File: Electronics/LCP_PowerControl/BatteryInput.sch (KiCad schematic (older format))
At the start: 0 parts

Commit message: Adding libraries and recent changes
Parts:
- added D?: D, symbol Device:D
- added J? (x5): Conn_01x02, Connector_PinSocket_2.54mm:PinSocket_1x02_P2.54mm_Vertical, symbol Connector_Generic:Conn_01x02
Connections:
- net BATT_V+: now also D?.1 (K), J?.2 (Pin_2), J?.2 (Pin_2), J?.2 (Pin_2), J?.2 (Pin_2)
- new net: D?.2 (A), J?.2 (Pin_2)
- new net GND: J?.1 (Pin_1), J?.1 (Pin_1), J?.1 (Pin_1), J?.1 (Pin_1), J?.1 (Pin_1)
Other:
- note added: "Battery #1 Connector"
- note added: "Battery #2 Connector"
- note added: "Battery #3 Connector"
- note added: "Battery #4 Connector"
- note added: "Battery Connections:\nExpected Battery Pack\n18SP1 Stacks, Alkaline, Diode Protected"
- note added: "External Power Connector\n(DC Supply)"
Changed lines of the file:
@@
 $Descr A4 11693 8268
 encoding utf-8
-Sheet 2 8
+Sheet 2 11
 Title ""
 Date ""
@@
 Comment4 ""
 $EndDescr
-Text HLabel 9500 2400 2    50   Output ~ 0
+Text HLabel 9600 1850 2    50   Output ~ 0
 BATT_V+
-Text HLabel 9500 2750 2    50   Input ~ 0
+Text HLabel 9600 1950 2    50   Input ~ 0
 BATT_V-
+$Comp
+L Connector_Generic:Conn_01x02 J?
+U 1 1 5EF29935
+P 3900 1950
+F 0 "J?" H 3818 1625 50  0000 C CNN
+F 1 "Conn_01x02" H 3818 1716 50  0000 C CNN
+F 2 "Connector_PinSocket_2.54mm:PinSocket_1x02_P2.54mm_Vertical" H 3900 1950 50  0001 C CNN
+F 3 "~" H 3900 1950 50  0001 C CNN
+	1    3900 1950
+	-1   0    0    1
+$EndComp
+$Comp
+L Connector_Generic:Conn_01x02 J?
+U 1 1 5EF2A22F
+P 3900 2850
+F 0 "J?" H 3818 2525 50  0000 C CNN
+F 1 "Conn_01x02" H 3818 2616 50  0000 C CNN
+F 2 "Connector_PinSocket_2.54mm:PinSocket_1x02_P2.54mm_Vertical" H 3900 2850 50  0001 C CNN
+F 3 "~" H 3900 2850 50  0001 C CNN
+	1    3900 2850
+	-1   0    0    1
+$EndComp
+$Comp
+L Connector_Generic:Conn_01x02 J?
+U 1 1 5EF2A6FE
+P 3900 3850
+F 0 "J?" H 3818 3525 50  0000 C CNN
+F 1 "Conn_01x02" H 3818 3616 50  0000 C CNN
+F 2 "Connector_PinSocket_2.54mm:PinSocket_1x02_P2.54mm_Vertical" H 3900 3850 50  0001 C CNN
+F 3 "~" H 3900 3850 50  0001 C CNN
+	1    3900 3850
+	-1   0    0    1
+$EndComp
+$Comp
+L Connector_Generic:Conn_01x02 J?
+U 1 1 5EF2AC09
+P 3900 4850
+F 0 "J?" H 3818 4525 50  0000 C CNN
+F 1 "Conn_01x02" H 3818 4616 50  0000 C CNN
+F 2 "Connector_PinSocket_2.54mm:PinSocket_1x02_P2.54mm_Vertical" H 3900 4850 50  0001 C CNN
+F 3 "~" H 3900 4850 50  0001 C CNN
+	1    3900 4850
+	-1   0    0    1
+$EndComp
+$Comp
+L Connector_Generic:Conn_01x02 J?
+U 1 1 5EF2B236
+P 3900 5950
+F 0 "J?" H 3818 5625 50  0000 C CNN
+F 1 "Conn_01x02" H 3818 5716 50  0000 C CNN
+F 2 "Connector_PinSocket_2.54mm:PinSocket_1x02_P2.54mm_Vertical" H 3900 5950 50  0001 C CNN
+F 3 "~" H 3900 5950 50  0001 C CNN
+	1    3900 5950
+	-1   0    0    1
+$EndComp
+$Comp
+L Device:D D?
+U 1 1 5EF2F687
+P 5150 5850
+F 0 "D?" H 5150 6066 50  0000 C CNN
+F 1 "D" H 5150 5975 50  0000 C CNN
+F 2 "" H 5150 5850 50  0001 C CNN
+F 3 "~" H 5150 5850 50  0001 C CNN
+	1    5150 5850
+	-1   0    0    -1
+$EndComp
+Wire Wire Line
+	4100 5950 4450 5950
+Wire Wire Line
+	4450 5950 4450 4850
+Wire Wire Line
+	4450 1950 4100 1950
+Wire Wire Line
+	4100 2850 4450 2850
+Connection ~ 4450 2850
+Wire Wire Line
+	4450 2850 4450 1950
+Wire Wire Line
+	4100 3850 4450 3850
+Connection ~ 4450 3850
+Wire Wire Line
+	4450 3850 4450 2850
+Wire Wire Line
+	4100 4850 4450 4850
+Connection ~ 4450 4850
+Wire Wire Line
+	4450 4850 4450 3850
+$Comp
+L power:GND #PWR?
+U 1 1 5EF31DCF
+P 4450 6300
+F 0 "#PWR?" H 4450 6050 50  0001 C CNN
+F 1 "GND" H 4455 6127 50  0000 C CNN
+F 2 "" H 4450 6300 50  0001 C CNN
+F 3 "" H 4450 6300 50  0001 C CNN
+	1    4450 6300
+	1    0    0    -1
+$EndComp
+Wire Wire Line
+	4450 6300 4450 5950
+Connection ~ 4450 5950
+Wire Wire Line
+	4100 5850 5000 5850
+Wire Wire Line
+	4100 4750 5650 4750
+Wire Wire Line
+	5650 4750 5650 5850
+Wire Wire Line
+	5650 5850 5300 5850
+Wire Wire Line
+	4100 3750 5650 3750
+Wire Wire Line
+	5650 3750 5650 4750
+Connection ~ 5650 4750
+Wire Wire Line
+	5650 2750 5650 3750
+Connection ~ 5650 3750
+Wire Wire Line
+	4100 2750 5650 2750
+Wire Wire Line
+	4100 1850 5650 1850
+Connection ~ 5650 2750
+Wire Wire Line
+	9600 1850 5650 1850
+Connection ~ 5650 1850
+Wire Wire Line
+	5650 1850 5650 2750
+Wire Wire Line
+	9600 1950 4450 1950
+Connection ~ 4450 1950
+Text Notes 2650 5950 0    50   ~ 0
+External Power Connector\n(DC Supply)
+Text Notes 2850 1950 0    50   ~ 0
+Battery #1 Connector
+Text Notes 2850 2850 0    50   ~ 0
+Battery #2 Connector
+Text Notes 2850 3800 0    50   ~ 0
+Battery #3 Connector
+Text Notes 2850 4800 0    50   ~ 0
+Battery #4 Connector
+Text Notes 1050 1300 0    50   ~ 0
+Battery Connections:\nExpected Battery Pack\n18SP1 Stacks, Alkaline, Diode Protected
 $EndSCHEMATC

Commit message: Aiming for rev 0.1 complete
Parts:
- added TP22, TP23: TestPoint, TestPoint:TestPoint_Keystone_5000-5004_Miniature, symbol Connector:TestPoint
- D5: renamed from D?; footprint (none) -> Diode_SMD:D_SMA; MPN (none) -> SK53A-LTP
- J10, J11, J12, J3, J9: renamed from J?; footprint Connector_PinSocket_2.54mm:PinSocket_1x02_P2.54mm_Vertical -> Connector_Molex:Molex_Micro-Fit_3.0_43045-0200_2x01_P3.00mm_Horizontal
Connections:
- net BATT_V+: now also TP22.1
- net GND: now also TP23.1
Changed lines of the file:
@@
 Sheet 2 11
 Title ""
-Date ""
-Rev ""
+Date "2020-06-17"
+Rev "R0.1"
 Comp ""
-Comment1 ""
+Comment1 "Design by: Matt Casari"
 Comment2 ""
 Comment3 ""
@@
 BATT_V-
 $Comp
-L Connector_Generic:Conn_01x02 J?
+L Connector_Generic:Conn_01x02 J3
 U 1 1 5EF29935
 P 3900 1950
-F 0 "J?" H 3818 1625 50  0000 C CNN
+F 0 "J3" H 3818 1625 50  0000 C CNN
 F 1 "Conn_01x02" H 3818 1716 50  0000 C CNN
-F 2 "Connector_PinSocket_2.54mm:PinSocket_1x02_P2.54mm_Vertical" H 3900 1950 50  0001 C CNN
+F 2 "Connector_Molex:Molex_Micro-Fit_3.0_43045-0200_2x01_P3.00mm_Horizontal" H 3900 1950 50  0001 C CNN
 F 3 "~" H 3900 1950 50  0001 C CNN
 	1    3900 1950
@@
 $EndComp
 $Comp
-L Connector_Generic:Conn_01x02 J?
+L Connector_Generic:Conn_01x02 J9
 U 1 1 5EF2A22F
 P 3900 2850
-F 0 "J?" H 3818 2525 50  0000 C CNN
+F 0 "J9" H 3818 2525 50  0000 C CNN
 F 1 "Conn_01x02" H 3818 2616 50  0000 C CNN
-F 2 "Connector_PinSocket_2.54mm:PinSocket_1x02_P2.54mm_Vertical" H 3900 2850 50  0001 C CNN
+F 2 "Connector_Molex:Molex_Micro-Fit_3.0_43045-0200_2x01_P3.00mm_Horizontal" H 3900 2850 50  0001 C CNN
 F 3 "~" H 3900 2850 50  0001 C CNN
 	1    3900 2850
@@
 $EndComp
 $Comp
-L Connector_Generic:Conn_01x02 J?
+L Connector_Generic:Conn_01x02 J10
 U 1 1 5EF2A6FE
 P 3900 3850
-F 0 "J?" H 3818 3525 50  0000 C CNN
+F 0 "J10" H 3818 3525 50  0000 C CNN
 F 1 "Conn_01x02" H 3818 3616 50  0000 C CNN
-F 2 "Connector_PinSocket_2.54mm:PinSocket_1x02_P2.54mm_Vertical" H 3900 3850 50  0001 C CNN
+F 2 "Connector_Molex:Molex_Micro-Fit_3.0_43045-0200_2x01_P3.00mm_Horizontal" H 3900 3850 50  0001 C CNN
 F 3 "~" H 3900 3850 50  0001 C CNN
 	1    3900 3850
@@
 $EndComp
 $Comp
-L Connector_Generic:Conn_01x02 J?
+L Connector_Generic:Conn_01x02 J11
 U 1 1 5EF2AC09
 P 3900 4850
-F 0 "J?" H 3818 4525 50  0000 C CNN
+F 0 "J11" H 3818 4525 50  0000 C CNN
 F 1 "Conn_01x02" H 3818 4616 50  0000 C CNN
-F 2 "Connector_PinSocket_2.54mm:PinSocket_1x02_P2.54mm_Vertical" H 3900 4850 50  0001 C CNN
+F 2 "Connector_Molex:Molex_Micro-Fit_3.0_43045-0200_2x01_P3.00mm_Horizontal" H 3900 4850 50  0001 C CNN
 F 3 "~" H 3900 4850 50  0001 C CNN
 	1    3900 4850
@@
 $EndComp
 $Comp
-L Connector_Generic:Conn_01x02 J?
+L Connector_Generic:Conn_01x02 J12
 U 1 1 5EF2B236
 P 3900 5950
-F 0 "J?" H 3818 5625 50  0000 C CNN
+F 0 "J12" H 3818 5625 50  0000 C CNN
 F 1 "Conn_01x02" H 3818 5716 50  0000 C CNN
-F 2 "Connector_PinSocket_2.54mm:PinSocket_1x02_P2.54mm_Vertical" H 3900 5950 50  0001 C CNN
+F 2 "Connector_Molex:Molex_Micro-Fit_3.0_43045-0200_2x01_P3.00mm_Horizontal" H 3900 5950 50  0001 C CNN
 F 3 "~" H 3900 5950 50  0001 C CNN
 	1    3900 5950
@@
 $EndComp
 $Comp
-L Device:D D?
+L Device:D D5
 U 1 1 5EF2F687
 P 5150 5850
-F 0 "D?" H 5150 6066 50  0000 C CNN
+F 0 "D5" H 5150 6066 50  0000 C CNN
 F 1 "D" H 5150 5975 50  0000 C CNN
-F 2 "" H 5150 5850 50  0001 C CNN
+F 2 "Diode_SMD:D_SMA" H 5150 5850 50  0001 C CNN
 F 3 "~" H 5150 5850 50  0001 C CNN
+F 4 "SK53A-LTP" H 5150 5850 50  0001 C CNN "MPN"
 	1    5150 5850
 	-1   0    0    -1
@@
 	4450 4850 4450 3850
 $Comp
-L power:GND #PWR?
+L power:GND #PWR015
 U 1 1 5EF31DCF
 P 4450 6300
-F 0 "#PWR?" H 4450 6050 50  0001 C CNN
+F 0 "#PWR015" H 4450 6050 50  0001 C CNN
 F 1 "GND" H 4455 6127 50  0000 C CNN
 F 2 "" H 4450 6300 50  0001 C CNN
@@
 	4100 1850 5650 1850
 Connection ~ 5650 2750
-Wire Wire Line
-	9600 1850 5650 1850
 Connection ~ 5650 1850
 Wire Wire Line
 	5650 1850 5650 2750
-Wire Wire Line
-	9600 1950 4450 1950
 Connection ~ 4450 1950
 Text Notes 2650 5950 0    50   ~ 0
@@
 Text Notes 1050 1300 0    50   ~ 0
 Battery Connections:\nExpected Battery Pack\n18SP1 Stacks, Alkaline, Diode Protected
+$Comp
+L Connector:TestPoint TP?
+U 1 1 5F052069
+P 6600 1600
+AR Path="/5EE2A7AF/5F052069" Ref="TP?"  Part="1"
+AR Path="/5EE4388C/5F052069" Ref="TP?"  Part="1"
+AR Path="/5EE2A57D/5F052069" Ref="TP22"  Part="1"
+F 0 "TP22" H 6658 1718 50  0000 L CNN
+F 1 "TestPoint" H 6658 1627 50  0000 L CNN
+F 2 "TestPoint:TestPoint_Keystone_5000-5004_Miniature" H 6800 1600 50  0001 C CNN
+F 3 "~" H 6800 1600 50  0001 C CNN
+F 4 "5000" H 6600 1600 50  0001 C CNN "MPN"
+	1    6600 1600
+	1    0    0    -1
+$EndComp
+$Comp
+L Connector:TestPoint TP?
+U 1 1 5F052070
+P 7050 1600
+AR Path="/5EE2A7AF/5F052070" Ref="TP?"  Part="1"
+AR Path="/5EE4388C/5F052070" Ref="TP?"  Part="1"
+AR Path="/5EE2A57D/5F052070" Ref="TP23"  Part="1"
+F 0 "TP23" H 7108 1718 50  0000 L CNN
+F 1 "TestPoint" H 7108 1627 50  0000 L CNN
+F 2 "TestPoint:TestPoint_Keystone_5000-5004_Miniature" H 7250 1600 50  0001 C CNN
+F 3 "~" H 7250 1600 50  0001 C CNN
+F 4 "5001" H 7050 1600 50  0001 C CNN "MPN"
+	1    7050 1600
+	1    0    0    -1
+$EndComp
+Wire Wire Line
+	6600 1600 6600 1850
+Wire Wire Line
+	5650 1850 6600 1850
+Connection ~ 6600 1850
+Wire Wire Line
+	6600 1850 9600 1850
+Wire Wire Line
+	7050 1600 7050 1950
+Wire Wire Line
+	4450 1950 7050 1950
+Connection ~ 7050 1950
+Wire Wire Line
+	7050 1950 9600 1950
 $EndSCHEMATC

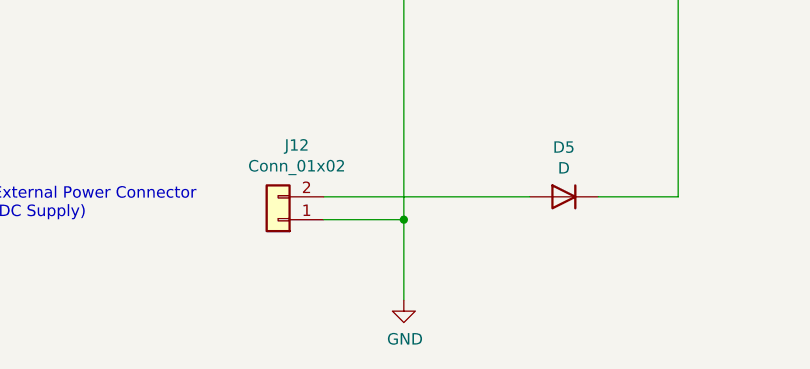
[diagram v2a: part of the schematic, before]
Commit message: KiCad Layout
Component and Traces finished. Need a look over. Will work on Silkscreen
after.

JTAG Connector. Should pin 1 be pulled up w/ 470Ohm resistor similar to
other designs? Also TDI and TMI signals are connected, is this correct?
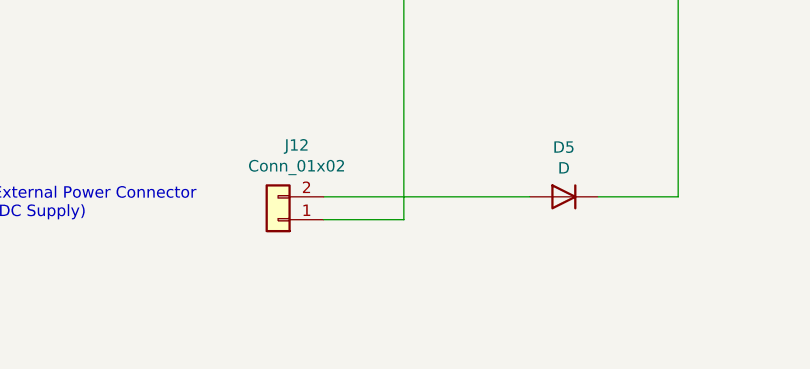
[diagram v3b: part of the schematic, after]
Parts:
- J10, J11, J12, J3, J9: footprint Connector_Molex:Molex_Micro-Fit_3.0_43045-0200_2x01_P3.00mm_Horizontal -> Connector_Molex:Molex_Micro-Fit_3.0_43045-0212_2x01_P3.00mm_Vertical
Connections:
- net GND renamed BATT_V-
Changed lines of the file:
@@
 F 0 "J3" H 3818 1625 50  0000 C CNN
 F 1 "Conn_01x02" H 3818 1716 50  0000 C CNN
-F 2 "Connector_Molex:Molex_Micro-Fit_3.0_43045-0200_2x01_P3.00mm_Horizontal" H 3900 1950 50  0001 C CNN
+F 2 "Connector_Molex:Molex_Micro-Fit_3.0_43045-0212_2x01_P3.00mm_Vertical" H 3900 1950 50  0001 C CNN
 F 3 "~" H 3900 1950 50  0001 C CNN
 	1    3900 1950
@@
 F 0 "J9" H 3818 2525 50  0000 C CNN
 F 1 "Conn_01x02" H 3818 2616 50  0000 C CNN
-F 2 "Connector_Molex:Molex_Micro-Fit_3.0_43045-0200_2x01_P3.00mm_Horizontal" H 3900 2850 50  0001 C CNN
+F 2 "Connector_Molex:Molex_Micro-Fit_3.0_43045-0212_2x01_P3.00mm_Vertical" H 3900 2850 50  0001 C CNN
 F 3 "~" H 3900 2850 50  0001 C CNN
 	1    3900 2850
@@
 F 0 "J10" H 3818 3525 50  0000 C CNN
 F 1 "Conn_01x02" H 3818 3616 50  0000 C CNN
-F 2 "Connector_Molex:Molex_Micro-Fit_3.0_43045-0200_2x01_P3.00mm_Horizontal" H 3900 3850 50  0001 C CNN
+F 2 "Connector_Molex:Molex_Micro-Fit_3.0_43045-0212_2x01_P3.00mm_Vertical" H 3900 3850 50  0001 C CNN
 F 3 "~" H 3900 3850 50  0001 C CNN
 	1    3900 3850
@@
 F 0 "J11" H 3818 4525 50  0000 C CNN
 F 1 "Conn_01x02" H 3818 4616 50  0000 C CNN
-F 2 "Connector_Molex:Molex_Micro-Fit_3.0_43045-0200_2x01_P3.00mm_Horizontal" H 3900 4850 50  0001 C CNN
+F 2 "Connector_Molex:Molex_Micro-Fit_3.0_43045-0212_2x01_P3.00mm_Vertical" H 3900 4850 50  0001 C CNN
 F 3 "~" H 3900 4850 50  0001 C CNN
 	1    3900 4850
@@
 F 0 "J12" H 3818 5625 50  0000 C CNN
 F 1 "Conn_01x02" H 3818 5716 50  0000 C CNN
-F 2 "Connector_Molex:Molex_Micro-Fit_3.0_43045-0200_2x01_P3.00mm_Horizontal" H 3900 5950 50  0001 C CNN
+F 2 "Connector_Molex:Molex_Micro-Fit_3.0_43045-0212_2x01_P3.00mm_Vertical" H 3900 5950 50  0001 C CNN
 F 3 "~" H 3900 5950 50  0001 C CNN
 	1    3900 5950
@@
 Wire Wire Line
 	4450 4850 4450 3850
-$Comp
-L power:GND #PWR015
-U 1 1 5EF31DCF
-P 4450 6300
-F 0 "#PWR015" H 4450 6050 50  0001 C CNN
-F 1 "GND" H 4455 6127 50  0000 C CNN
-F 2 "" H 4450 6300 50  0001 C CNN
-F 3 "" H 4450 6300 50  0001 C CNN
-	1    4450 6300
-	1    0    0    -1
-$EndComp
-Wire Wire Line
-	4450 6300 4450 5950
-Connection ~ 4450 5950
 Wire Wire Line
 	4100 5850 5000 5850

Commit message: LCP_PowerControl Rev1
Board layout in Kicad.
Gerbers.
BOM
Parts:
- J10, J11, J12, J3, J9: MPN (none) -> 0430450227
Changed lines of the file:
@@
 F 2 "Connector_Molex:Molex_Micro-Fit_3.0_43045-0212_2x01_P3.00mm_Vertical" H 3900 1950 50  0001 C CNN
 F 3 "~" H 3900 1950 50  0001 C CNN
+F 4 "0430450227" H 3900 1950 50  0001 C CNN "MPN"
 	1    3900 1950
 	-1   0    0    1
@@
 F 2 "Connector_Molex:Molex_Micro-Fit_3.0_43045-0212_2x01_P3.00mm_Vertical" H 3900 2850 50  0001 C CNN
 F 3 "~" H 3900 2850 50  0001 C CNN
+F 4 "0430450227" H 3900 2850 50  0001 C CNN "MPN"
 	1    3900 2850
 	-1   0    0    1
@@
 F 2 "Connector_Molex:Molex_Micro-Fit_3.0_43045-0212_2x01_P3.00mm_Vertical" H 3900 3850 50  0001 C CNN
 F 3 "~" H 3900 3850 50  0001 C CNN
+F 4 "0430450227" H 3900 3850 50  0001 C CNN "MPN"
 	1    3900 3850
 	-1   0    0    1
@@
 F 2 "Connector_Molex:Molex_Micro-Fit_3.0_43045-0212_2x01_P3.00mm_Vertical" H 3900 4850 50  0001 C CNN
 F 3 "~" H 3900 4850 50  0001 C CNN
+F 4 "0430450227" H 3900 4850 50  0001 C CNN "MPN"
 	1    3900 4850
 	-1   0    0    1
@@
 F 2 "Connector_Molex:Molex_Micro-Fit_3.0_43045-0212_2x01_P3.00mm_Vertical" H 3900 5950 50  0001 C CNN
 F 3 "~" H 3900 5950 50  0001 C CNN
+F 4 "0430450227" H 3900 5950 50  0001 C CNN "MPN"
 	1    3900 5950
 	-1   0    0    1

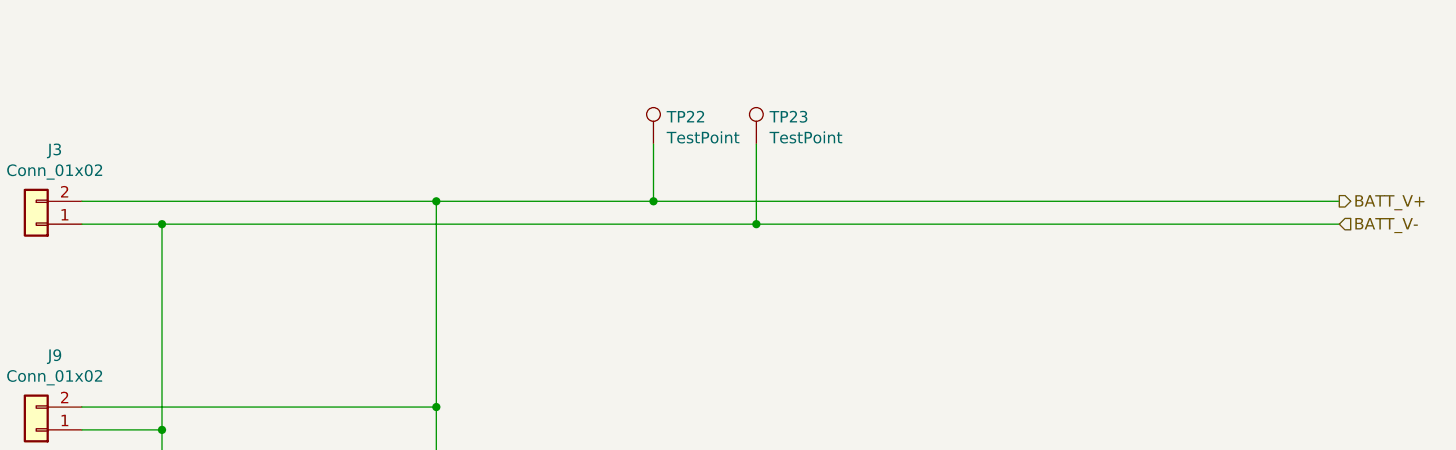
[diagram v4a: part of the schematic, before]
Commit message: Rev1
Removed test points. Cleaned up unnecessary traces. Fixed electrical issues #1-#7
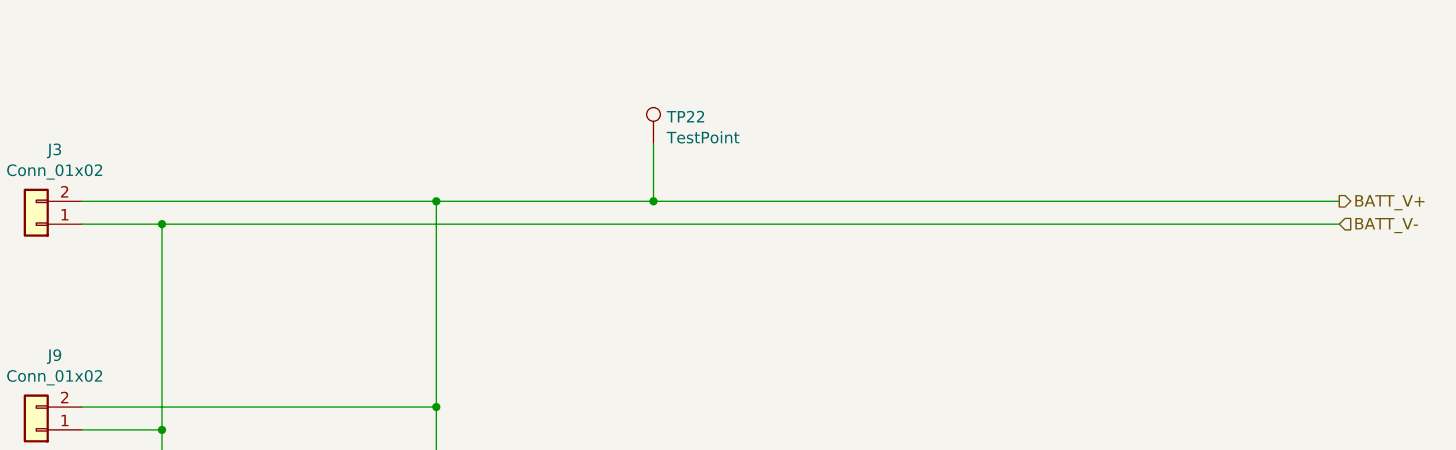
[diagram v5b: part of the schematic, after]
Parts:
- removed TP23: TestPoint, TestPoint:TestPoint_Keystone_5000-5004_Miniature, symbol Connector:TestPoint
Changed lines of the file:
@@
 Text Notes 1050 1300 0    50   ~ 0
 Battery Connections:\nExpected Battery Pack\n18SP1 Stacks, Alkaline, Diode Protected
+Wire Wire Line
+	6600 1850 9600 1850
+Wire Wire Line
+	5650 1850 6600 1850
+Connection ~ 6600 1850
+Wire Wire Line
+	6600 1600 6600 1850
 $Comp
 L Connector:TestPoint TP?
@@
 	1    0    0    -1
 $EndComp
-$Comp
-L Connector:TestPoint TP?
-U 1 1 5F052070
-P 7050 1600
-AR Path="/5EE2A7AF/5F052070" Ref="TP?"  Part="1"
-AR Path="/5EE4388C/5F052070" Ref="TP?"  Part="1"
-AR Path="/5EE2A57D/5F052070" Ref="TP23"  Part="1"
-F 0 "TP23" H 7108 1718 50  0000 L CNN
-F 1 "TestPoint" H 7108 1627 50  0000 L CNN
-F 2 "TestPoint:TestPoint_Keystone_5000-5004_Miniature" H 7250 1600 50  0001 C CNN
-F 3 "~" H 7250 1600 50  0001 C CNN
-F 4 "5001" H 7050 1600 50  0001 C CNN "MPN"
-	1    7050 1600
-	1    0    0    -1
-$EndComp
 Wire Wire Line
-	6600 1600 6600 1850
-Wire Wire Line
-	5650 1850 6600 1850
-Connection ~ 6600 1850
-Wire Wire Line
-	6600 1850 9600 1850
-Wire Wire Line
-	7050 1600 7050 1950
-Wire Wire Line
-	4450 1950 7050 1950
-Connection ~ 7050 1950
-Wire Wire Line
-	7050 1950 9600 1950
+	4450 1950 9600 1950
 $EndSCHEMATC

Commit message: BOM Update
Updated MPNs on components to match supplies as well as correcting some resistor values
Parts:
- J10, J11, J12, J3, J9: MPN 0430450227 -> 0430450213
- TP22: MPN 5000 -> (none)
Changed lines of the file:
@@
 F 2 "Connector_Molex:Molex_Micro-Fit_3.0_43045-0212_2x01_P3.00mm_Vertical" H 3900 1950 50  0001 C CNN
 F 3 "~" H 3900 1950 50  0001 C CNN
-F 4 "0430450227" H 3900 1950 50  0001 C CNN "MPN"
+F 4 "0430450213" H 3900 1950 50  0001 C CNN "MPN"
 	1    3900 1950
 	-1   0    0    1
@@
 F 2 "Connector_Molex:Molex_Micro-Fit_3.0_43045-0212_2x01_P3.00mm_Vertical" H 3900 2850 50  0001 C CNN
 F 3 "~" H 3900 2850 50  0001 C CNN
-F 4 "0430450227" H 3900 2850 50  0001 C CNN "MPN"
+F 4 "0430450213" H 3900 2850 50  0001 C CNN "MPN"
 	1    3900 2850
 	-1   0    0    1
@@
 F 2 "Connector_Molex:Molex_Micro-Fit_3.0_43045-0212_2x01_P3.00mm_Vertical" H 3900 3850 50  0001 C CNN
 F 3 "~" H 3900 3850 50  0001 C CNN
-F 4 "0430450227" H 3900 3850 50  0001 C CNN "MPN"
+F 4 "0430450213" H 3900 3850 50  0001 C CNN "MPN"
 	1    3900 3850
 	-1   0    0    1
@@
 F 2 "Connector_Molex:Molex_Micro-Fit_3.0_43045-0212_2x01_P3.00mm_Vertical" H 3900 4850 50  0001 C CNN
 F 3 "~" H 3900 4850 50  0001 C CNN
-F 4 "0430450227" H 3900 4850 50  0001 C CNN "MPN"
+F 4 "0430450213" H 3900 4850 50  0001 C CNN "MPN"
 	1    3900 4850
 	-1   0    0    1
@@
 F 2 "Connector_Molex:Molex_Micro-Fit_3.0_43045-0212_2x01_P3.00mm_Vertical" H 3900 5950 50  0001 C CNN
 F 3 "~" H 3900 5950 50  0001 C CNN
-F 4 "0430450227" H 3900 5950 50  0001 C CNN "MPN"
+F 4 "0430450213" H 3900 5950 50  0001 C CNN "MPN"
 	1    3900 5950
 	-1   0    0    1
@@
 F 2 "TestPoint:TestPoint_Keystone_5000-5004_Miniature" H 6800 1600 50  0001 C CNN
 F 3 "~" H 6800 1600 50  0001 C CNN
-F 4 "5000" H 6600 1600 50  0001 C CNN "MPN"
+F 4 "" H 6600 1600 50  0001 C CNN "MPN"
 	1    6600 1600
 	1    0    0    -1
